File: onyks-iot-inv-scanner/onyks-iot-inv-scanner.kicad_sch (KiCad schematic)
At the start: 14 parts, among them J1 Conn_01x24_MountingPin, SW1 EN, SW2 BOOT, U2 ESP32-S3-WROOM-1

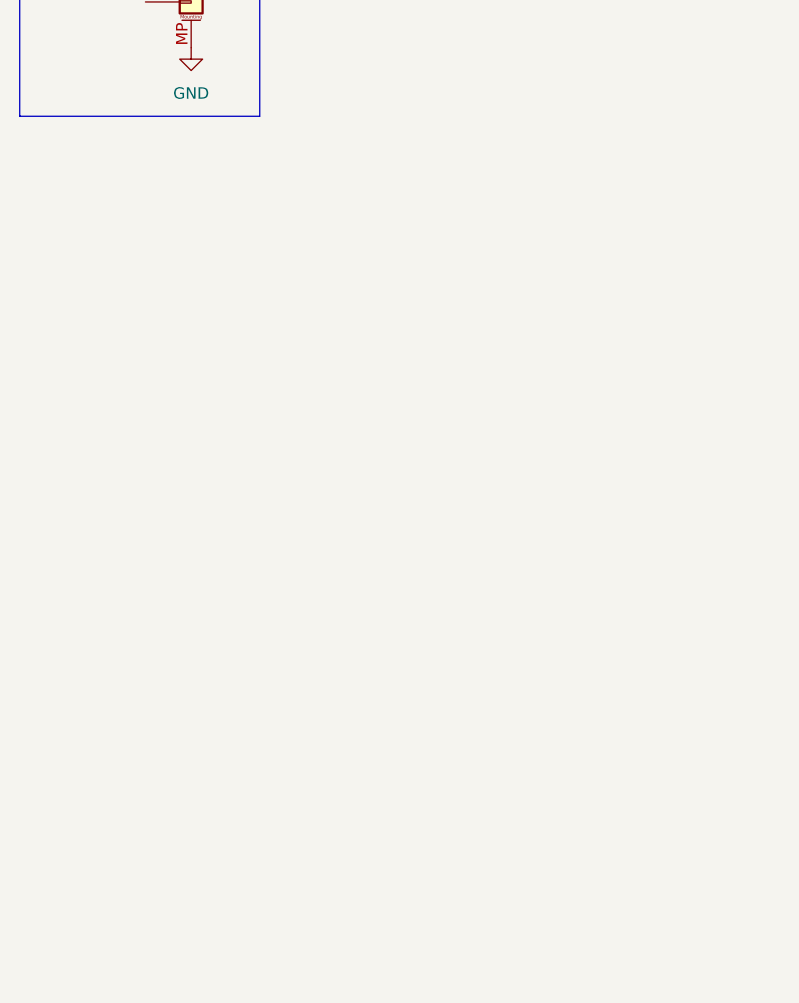
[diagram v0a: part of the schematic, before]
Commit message: added schematic for usb connector with default values
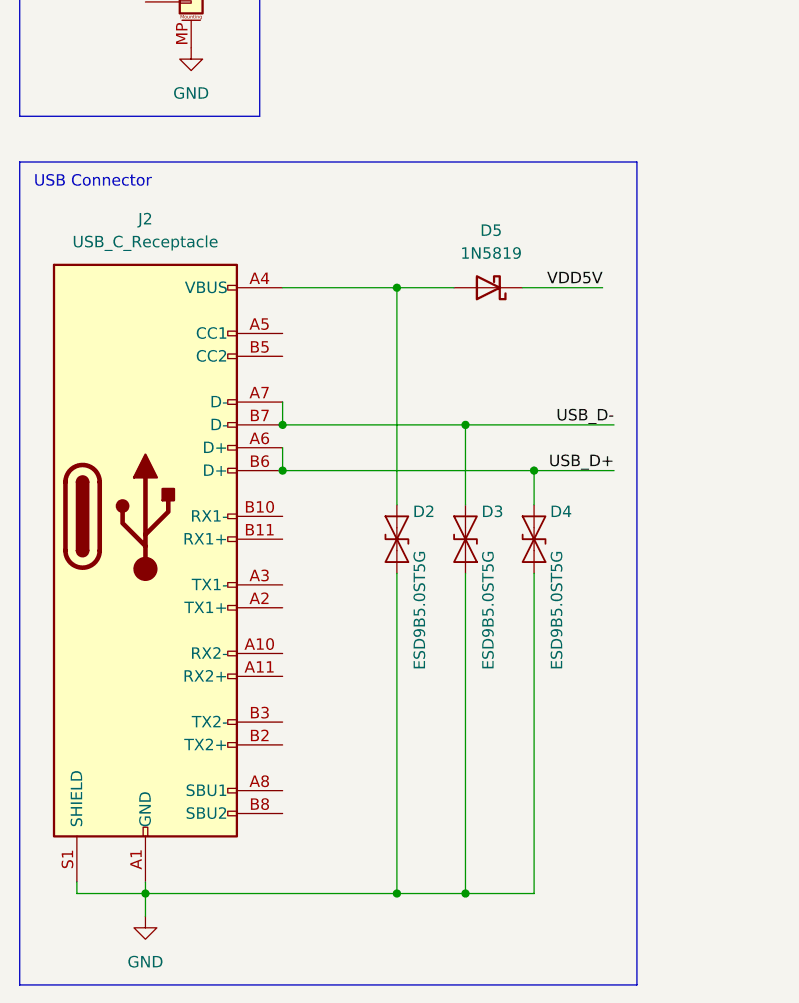
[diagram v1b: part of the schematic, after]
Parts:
- added D2, D3, D4: ESD9B5.0ST5G, Diode_SMD:D_SOD-923, symbol Diode:ESD9B5.0ST5G
- added D5: 1N5819, Diode_THT:D_DO-41_SOD81_P10.16mm_Horizontal, symbol Diode:1N5819
- added J2: USB_C_Receptacle, symbol Connector:USB_C_Receptacle
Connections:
- net GND: now also D2.1 (A1), D3.1 (A1), D4.1 (A1), J2.A1 (GND), J2.A12 (GND), J2.B1 (GND), J2.B12 (GND), J2.S1 (SHIELD)
- net USB_D+: now also D4.2 (A2), J2.A6 (D+), J2.B6 (D+)
- net USB_D-: now also D3.2 (A2), J2.A7 (D-), J2.B7 (D-)
- new net: D2.2 (A2), D5.2 (A), J2.A4 (VBUS), J2.A9 (VBUS), J2.B4 (VBUS), J2.B9 (VBUS)
- new net VDD5V: D5.1 (K)
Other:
- note added: "USB Connector"

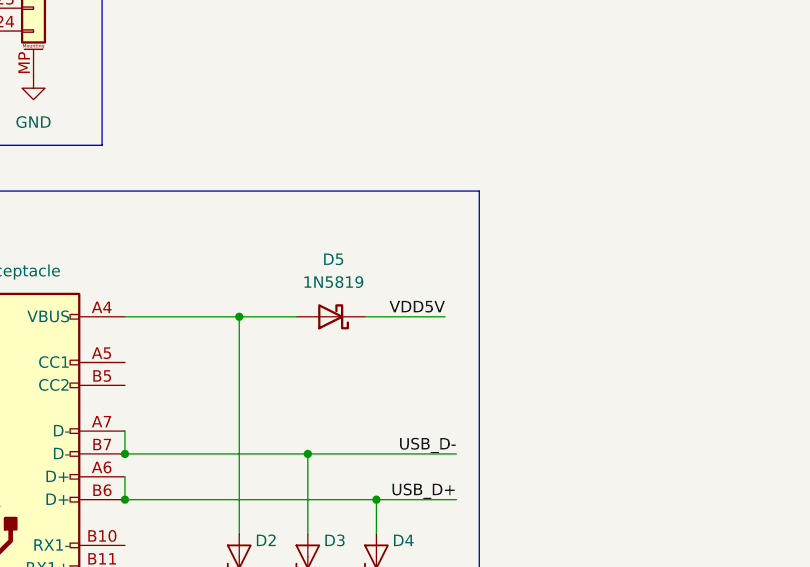
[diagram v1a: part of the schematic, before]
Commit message: fixed vcc label
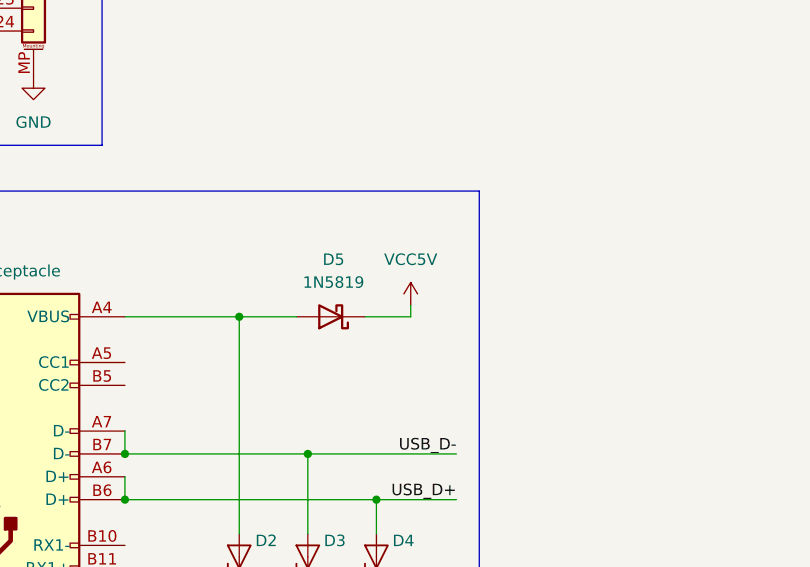
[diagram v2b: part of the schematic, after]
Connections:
- net VDD5V renamed VCC5V
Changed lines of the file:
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@@
 	(wire
 		(pts
+			(xy 76.2 113.03) (xy 76.2 114.3)
+		)
+		(stroke
+			(width 0)
+			(type default)
+		)
+	)
+	(wire
+		(pts
 			(xy 20.32 52.07) (xy 29.21 52.07)
 		)
@@
 	(wire
 		(pts
-			(xy 151.13 33.02) (xy 154.94 33.02)
+			(xy 71.12 114.3) (xy 76.2 114.3)
 		)
 		(stroke
@@
 	(wire
 		(pts
-			(xy 57.15 146.05) (xy 57.15 181.61)
+			(xy 151.13 33.02) (xy 154.94 33.02)
 		)
 		(stroke
@@
 	(wire
 		(pts
-			(xy 71.12 114.3) (xy 80.01 114.3)
+			(xy 57.15 146.05) (xy 57.15 181.61)
 		)
 		(stroke
@@
 		)
 	)
-	(label "VDD5V"
-		(at 80.01 114.3 180)
-		(effects
-			(font
-				(size 1.27 1.27)
-			)
-			(justify right bottom)
-		)
-	)
 	(label "Y9"
 		(at 20.32 54.61 0)
@@
 					(unit 1)
 				)
+			)
+		)
+	)
+	(symbol
+		(lib_id "power:VCC")
+		(at 76.2 113.03 0)
+		(unit 1)
+		(exclude_from_sim no)
+		(in_bom yes)
+		(on_board yes)
+		(dnp no)
+		(fields_autoplaced yes)
+		(property "Reference" "#PWR013"
+			(at 76.2 116.84 0)
+			(effects
+				(font
+					(size 1.27 1.27)
+				)
+				(hide yes)
+			)
+		)
+		(property "Value" "VCC5V"
+			(at 76.2 107.95 0)
+			(effects
+				(font
+					(size 1.27 1.27)
+				)
+			)
+		)
+		(property "Footprint" ""
+			(at 76.2 113.03 0)
+			(effects
+				(font
+					(size 1.27 1.27)
+				)
+				(hide yes)
+			)
+		)
+		(property "Datasheet" ""
+			(at 76.2 113.03 0)
+			(effects
+				(font
+					(size 1.27 1.27)
+				)
+				(hide yes)
+			)
+		)
+		(property "Description" "Power symbol creates a global label with name \"VCC\""
+			(at 76.2 113.03 0)
+			(effects
+				(font
+					(size 1.27 1.27)
+				)
+				(hide yes)
+			)
+		)
+		(pin "1"
+		)
+		(instances
+			(project ""
+				(path "/37956750-1b3c-4b3f-94c5-40fd1631cd50"
+					(reference "#PWR013")
+					(unit 1)
+				)

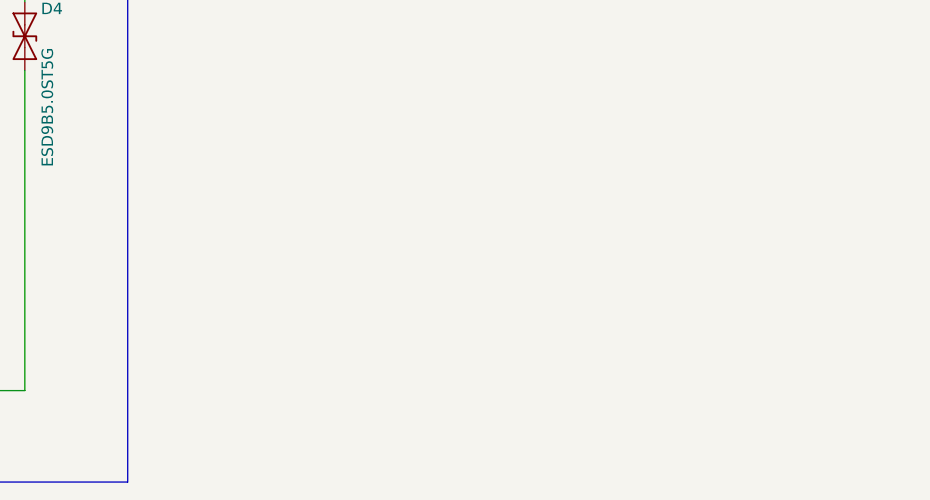
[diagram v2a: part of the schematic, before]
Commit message: added first schematics for battery
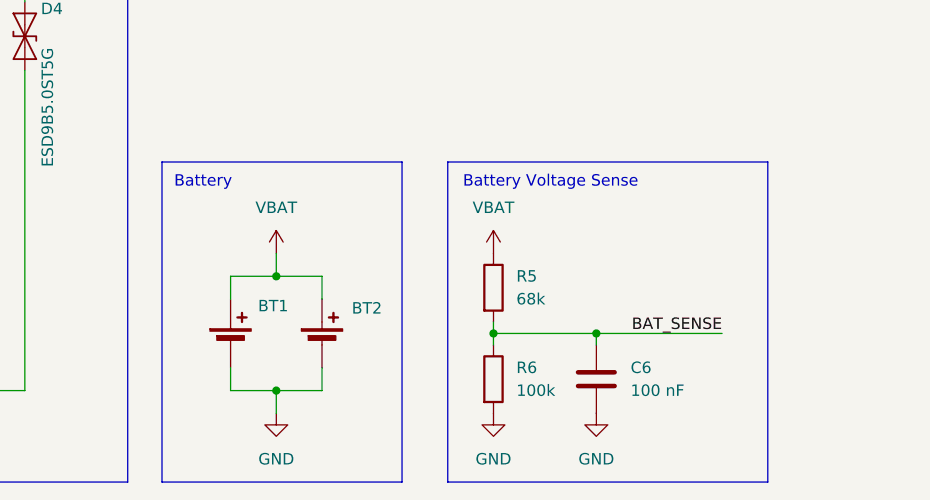
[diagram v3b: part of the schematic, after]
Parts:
- added BT1, BT2: Battery_Cell, symbol Device:Battery_Cell
- added C6: 100 nF, symbol Device:C
- added R5: 68k, symbol Device:R
- added R6: 100k, symbol Device:R
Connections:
- net GND: now also BT1.2 (-), BT2.2 (-), C6.2, R6.2
- new net BAT_SENSE: C6.1, R5.2, R6.1
- new net VBAT: BT1.1 (+), BT2.1 (+), R5.1
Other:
- note added: "Battery"
- note added: "Battery Voltage Sense"

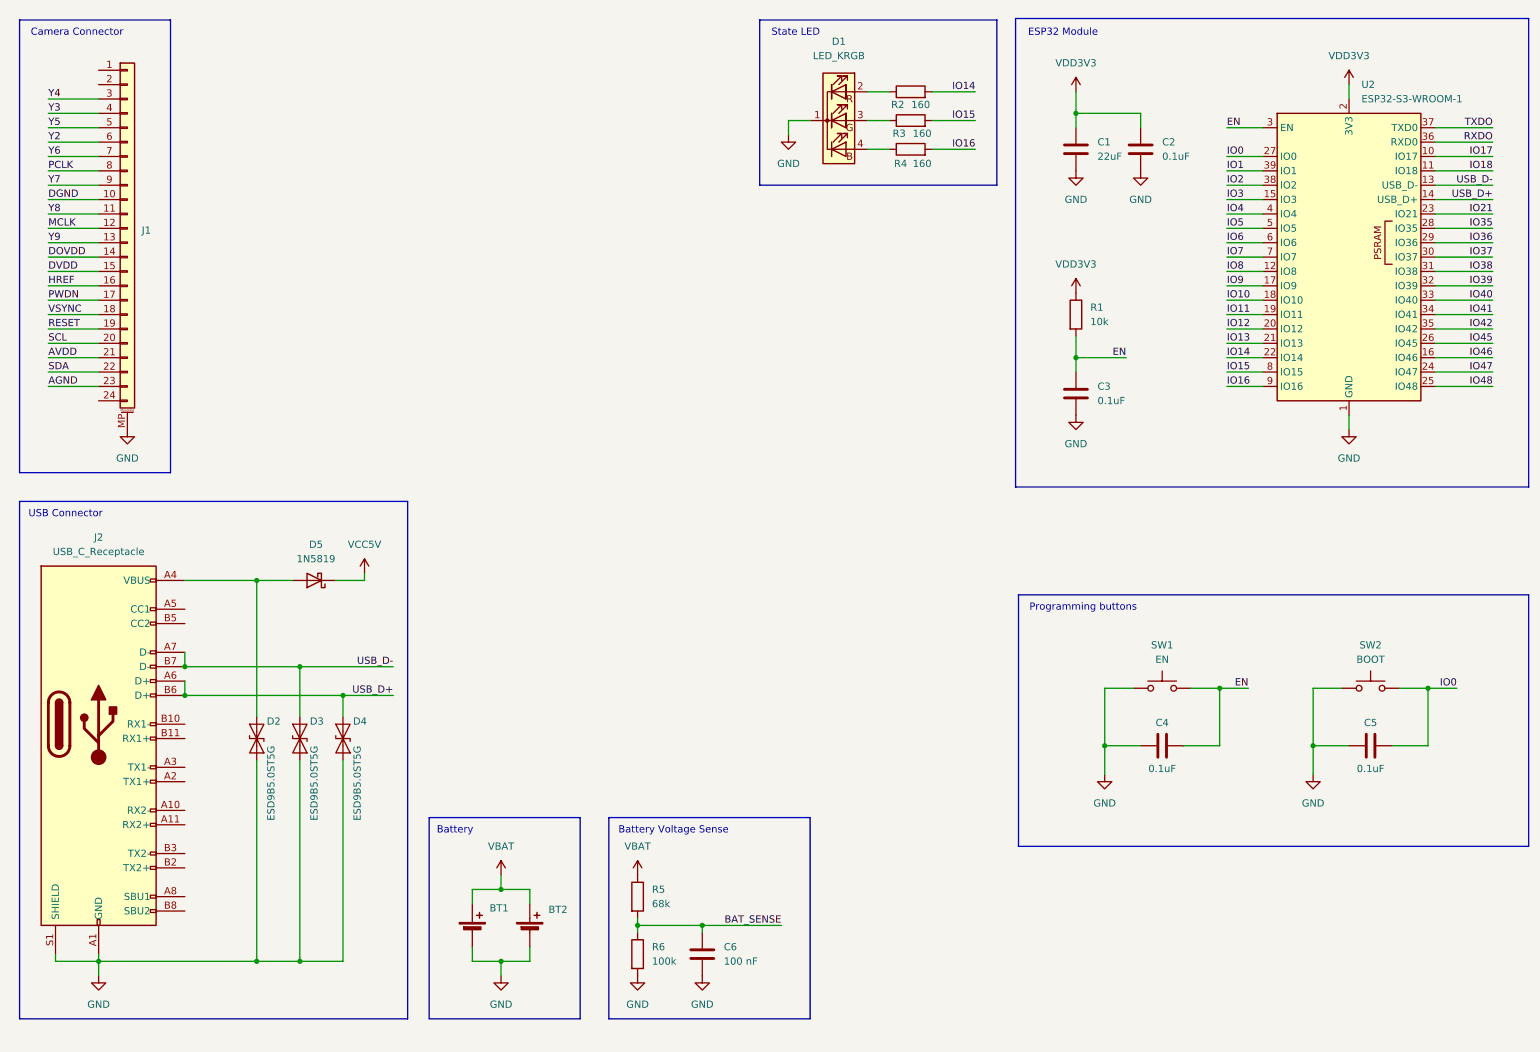
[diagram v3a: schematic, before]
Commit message: added battery protection and charging system
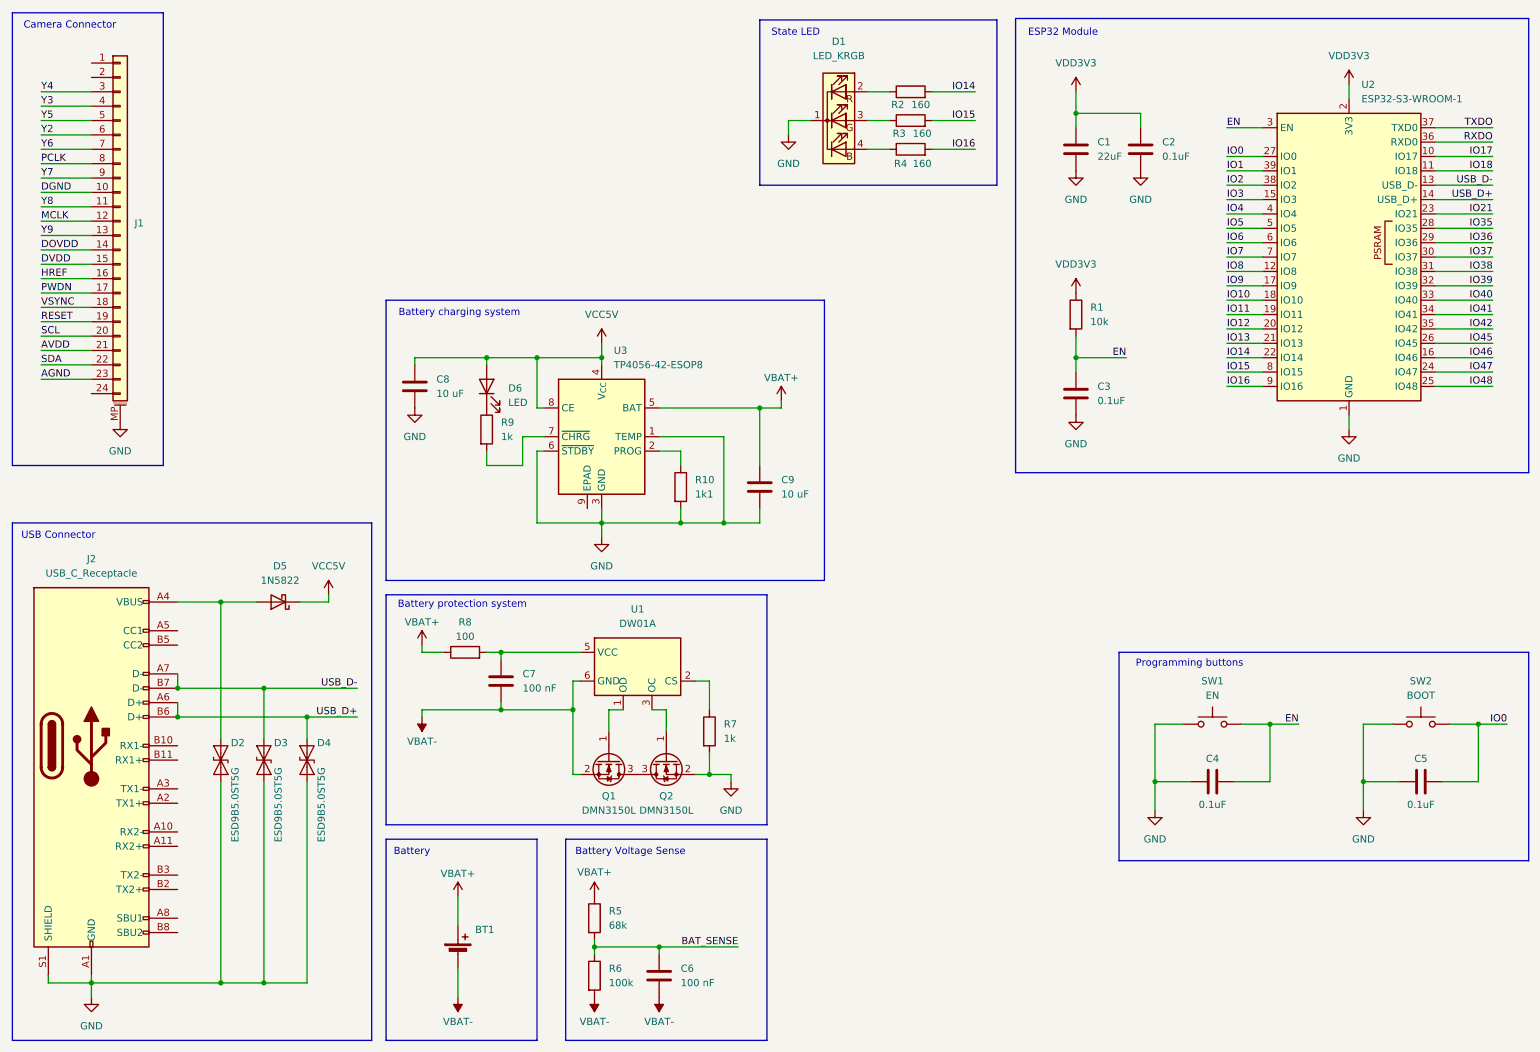
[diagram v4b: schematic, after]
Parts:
- removed BT2: Battery_Cell, symbol Device:Battery_Cell
- removed D5: 1N5819, Diode_THT:D_DO-41_SOD81_P10.16mm_Horizontal, symbol Diode:1N5819
- added C7: 100 nF, symbol Device:C
- added C8, C9: 10 uF, symbol Device:C
- added D5: 1N5822, Diode_THT:D_DO-201AD_P15.24mm_Horizontal, symbol Diode:1N5822
- added D6: LED, symbol Device:LED
- added Q1, Q2: DMN3150L, Package_TO_SOT_SMD:SOT-23, symbol Transistor_FET:DMN3150L
- added R10: 1k1, symbol Device:R
- added R7, R9: 1k, symbol Device:R
- added R8: 100, symbol Device:R
- added U1: DW01A, Package_TO_SOT_SMD:SOT-23-6, symbol Battery_Management:DW01A
- added U3: TP4056-42-ESOP8, Package_SO:SOIC-8-1EP_3.9x4.9mm_P1.27mm_EP2.41x3.3mm_ThermalVias, symbol Battery_Management:TP4056-42-ESOP8
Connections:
- net GND: now also C8.2, C9.2, Q2.2 (S), R10.2, R7.2, U3.1 (TEMP), U3.3 (GND), U3.6 (~{STDBY}); no longer BT1.2 (-), C6.2, R6.2
- net VCC5V: now also C8.1, D5.1 (K), D6.2 (A), U3.4 (V_{CC}), U3.8 (CE)
- net at D2.2 (A2), J2.A4 (VBUS), J2.A9 (VBUS)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: now also D5.2 (A)
- net VBAT renamed VBAT+
- net VBAT+: now also C9.1, R8.1, U3.5 (BAT)
- new net: Q1.1 (G), U1.1 (OD)
- new net: Q1.3 (D), Q2.3 (D)
- new net: R7.1, U1.2 (CS)
- new net: R10.1, U3.2 (PROG)
- new net: Q2.1 (G), U1.3 (OC)
- new net: C7.1, R8.2, U1.5 (VCC)
- new net: D6.1 (K), R9.1
- new net: R9.2, U3.7 (~{CHRG})
- new net VBAT-: BT1.2 (-), C6.2, C7.2, Q1.2 (S), R6.2, U1.6 (GND)
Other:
- note added: "Battery charging system"
- note added: "Battery protection system"
- moved on the sheet: BT1, C4, C5, C6, D2, D3, D4, J1, J2, R5, R6, SW1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

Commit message: moved some of schemes to hierarchical subplanes
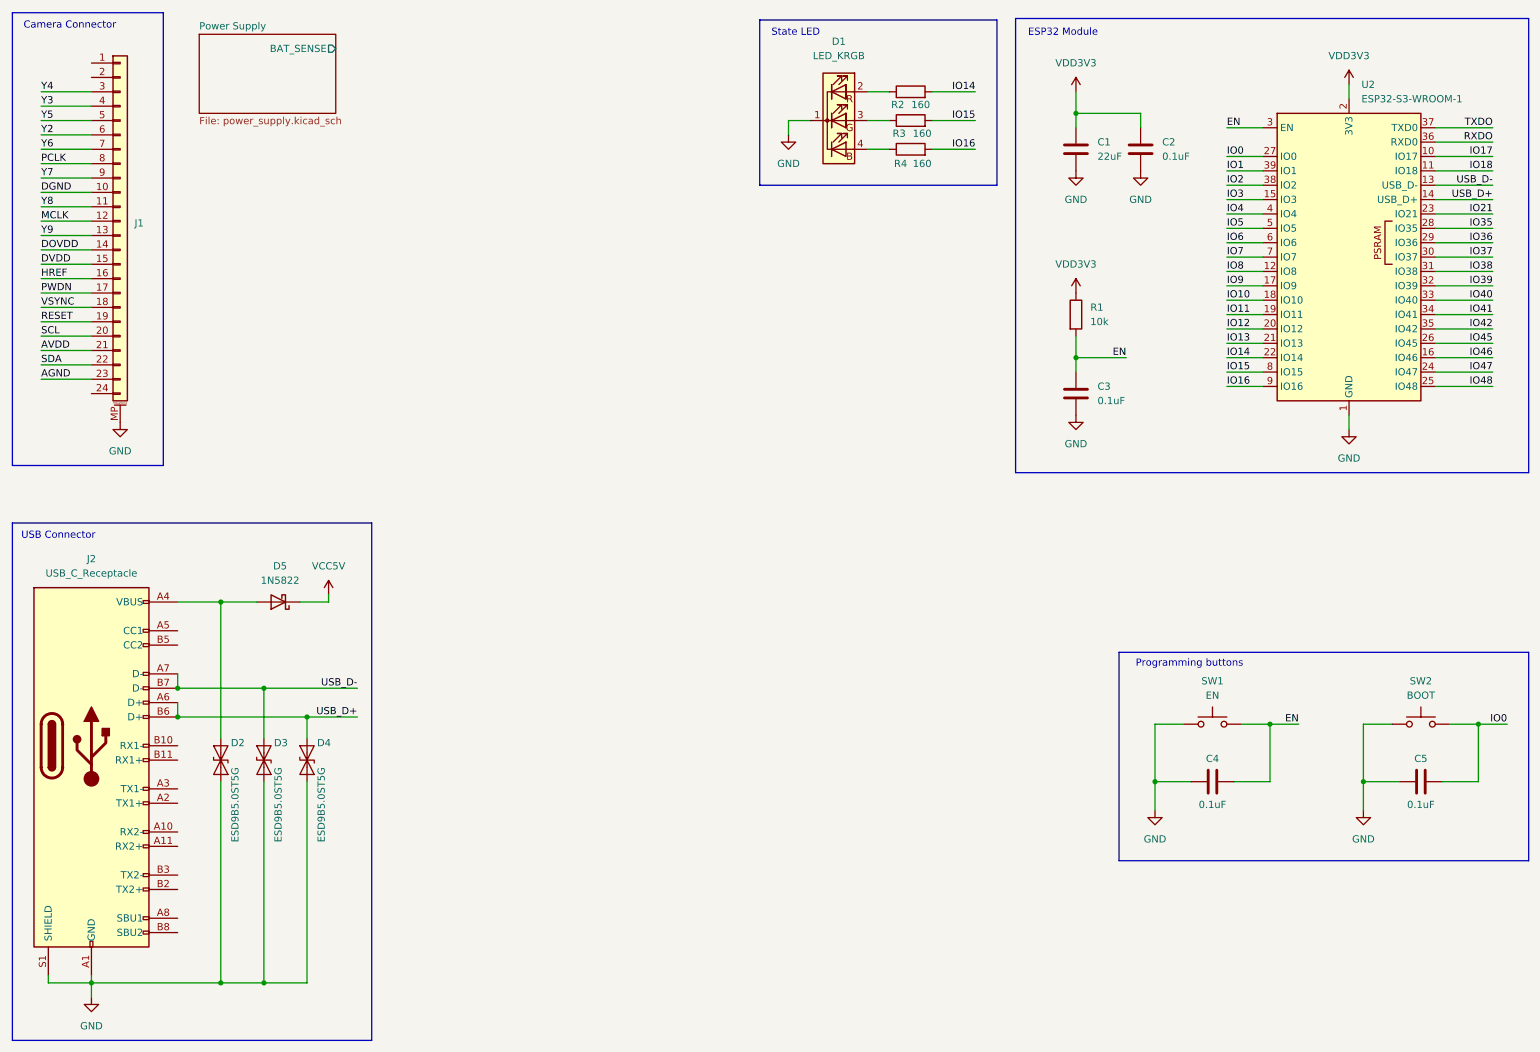
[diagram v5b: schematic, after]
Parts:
- removed BT1: Battery_Cell, symbol Device:Battery_Cell
- removed C6, C7: 100 nF, symbol Device:C
- removed C8, C9: 10 uF, symbol Device:C
- removed D6: LED, symbol Device:LED
- removed Q1, Q2: DMN3150L, Package_TO_SOT_SMD:SOT-23, symbol Transistor_FET:DMN3150L
- removed R10: 1k1, symbol Device:R
- removed R5: 68k, symbol Device:R
- removed R6: 100k, symbol Device:R
- removed R7, R9: 1k, symbol Device:R
- removed R8: 100, symbol Device:R
- removed U1: DW01A, Package_TO_SOT_SMD:SOT-23-6, symbol Battery_Management:DW01A
- removed U3: TP4056-42-ESOP8, Package_SO:SOIC-8-1EP_3.9x4.9mm_P1.27mm_EP2.41x3.3mm_ThermalVias, symbol Battery_Management:TP4056-42-ESOP8
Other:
- added sheet Power Supply (power_supply.kicad_sch)
- note removed: "Battery"
- note removed: "Battery Voltage Sense"
- note removed: "Battery charging system"
- note removed: "Battery protection system"
